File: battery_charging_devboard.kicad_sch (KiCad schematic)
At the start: 0 parts

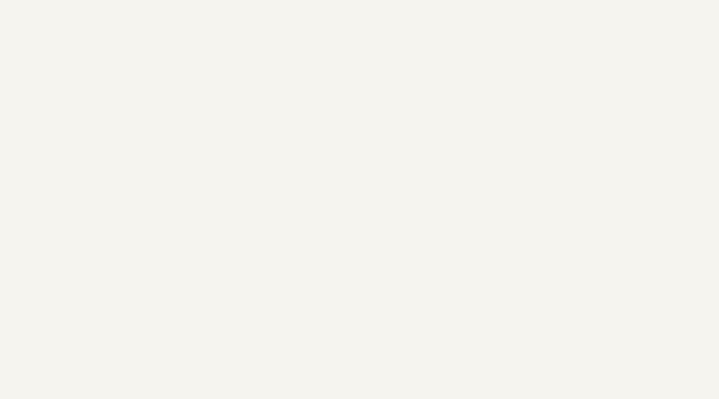
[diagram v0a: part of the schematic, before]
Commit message: Added microcontroller stage. Need to fix the supply routing to power from battery.
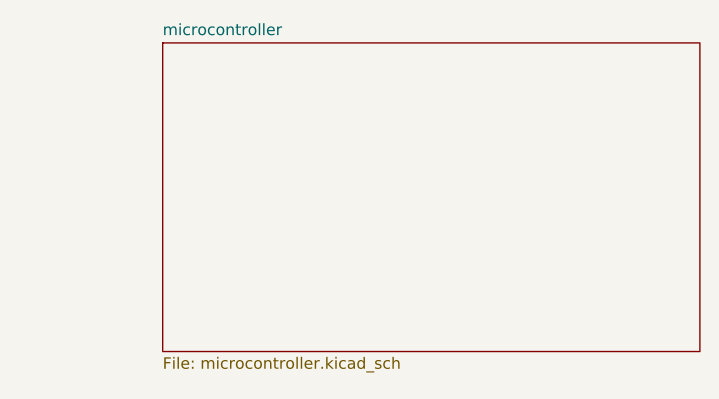
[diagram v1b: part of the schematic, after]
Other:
- added sheet microcontroller (microcontroller.kicad_sch)
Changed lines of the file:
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@@
 (kicad_sch (version 20230121) (generator eeschema)
   (paper "A4")
+  (sheet (at 198.755 32.385) (size 59.69 34.29) (fields_autoplaced)
+    (stroke (width 0.1524) (type solid))
+    (fill (color 0 0 0 0.0000))
+    (property "Sheetname" "microcontroller" (at 198.755 31.6734 0)
+      (effects (font (size 1.27 1.27)) (justify left bottom))
+    )
+    (property "Sheetfile" "microcontroller.kicad_sch" (at 198.755 67.2596 0)
+      (effects (font (size 1.27 1.27)) (justify left top))
+    )
+    (instances
+      (project "battery_charging_devboard"
+        (path "/451b7129-01d5-46cf-a4e9-c4e0c27ff0b6" (page "4"))
+      )
+    )
+  )
   (sheet (at 114.935 33.02) (size 57.785 34.29) (fields_autoplaced)
     (stroke (width 0.1524) (type solid))
